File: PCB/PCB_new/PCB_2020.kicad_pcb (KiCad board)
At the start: 2 copper layers, 102.2 x 94.5 mm, 26 parts, among them IC1 LM358N, Q1 220mA/50V/3.5Ω, Q2 100V/17A, Q3 100V/17A, Q4 100V/17A, Q5 100V/17A, Q6 100V/17A, U1 TI_CONN

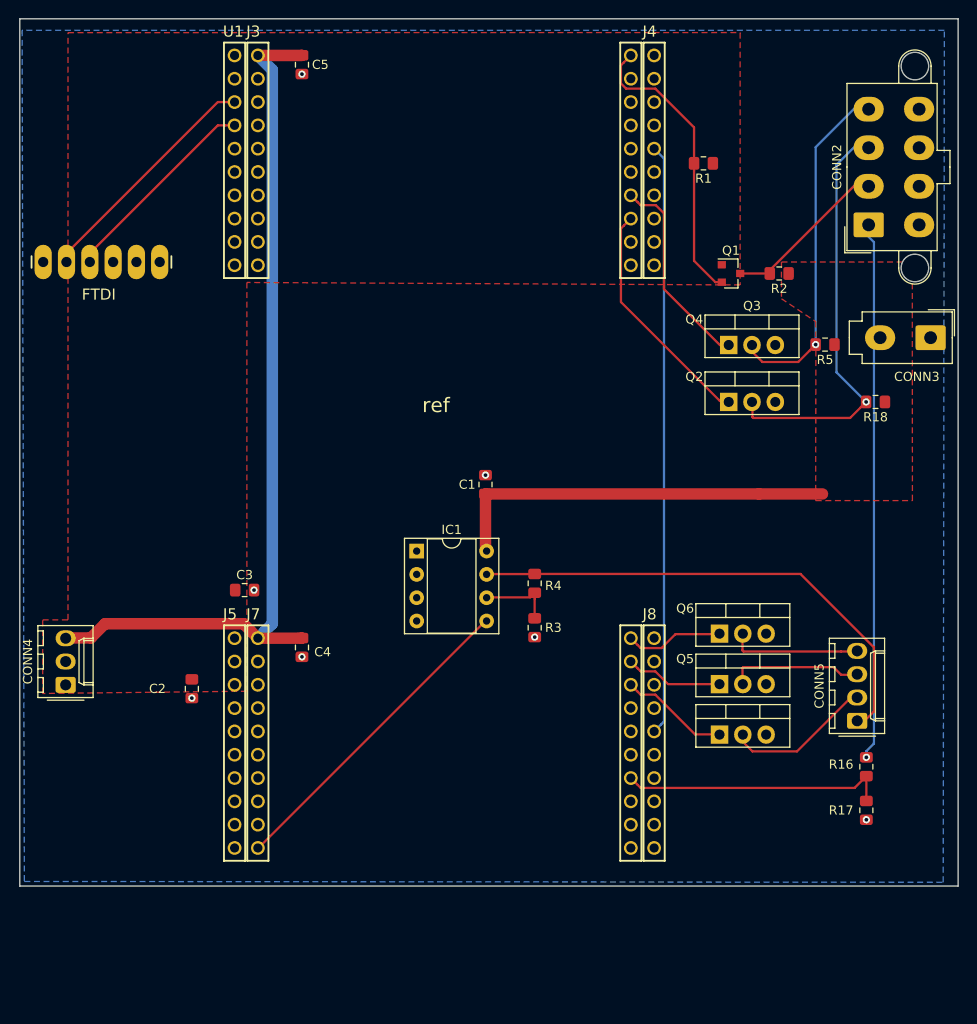
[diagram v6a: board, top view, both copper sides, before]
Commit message: moved components to keep proper space for ti
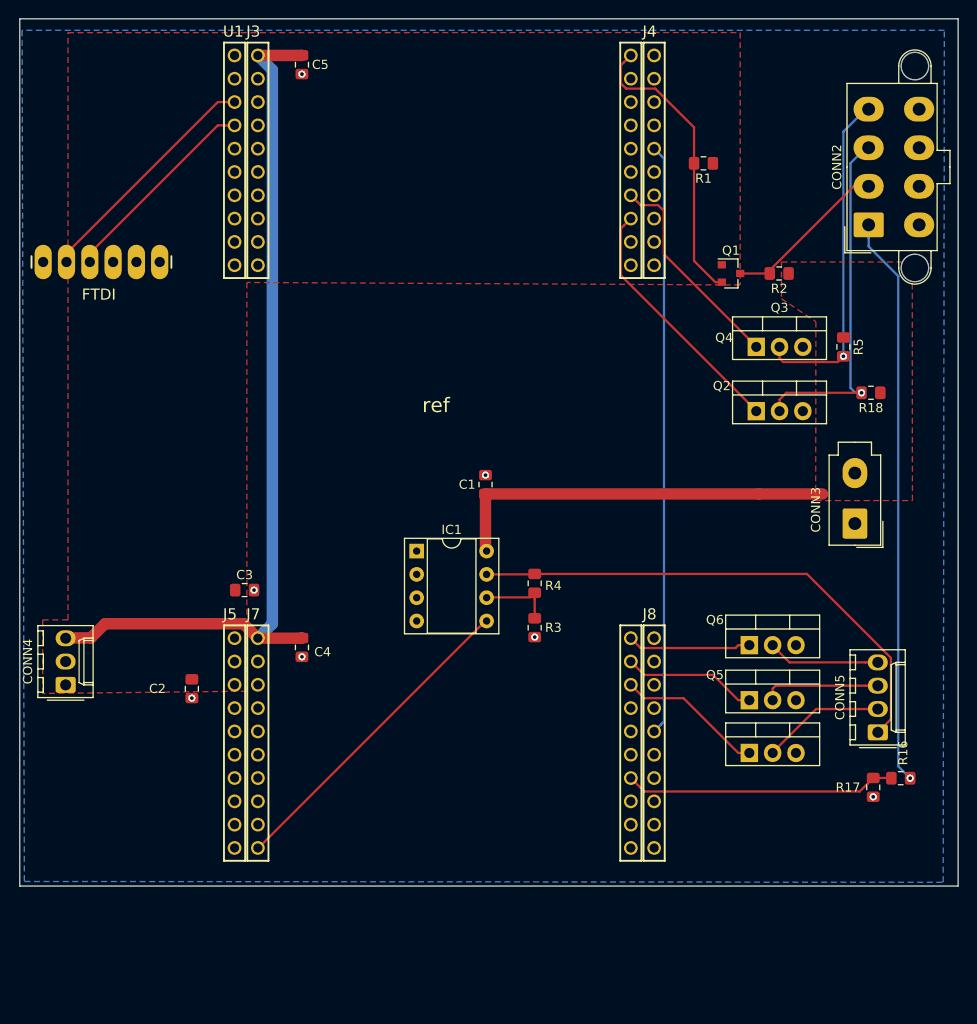
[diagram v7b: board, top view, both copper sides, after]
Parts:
- moved CONN3 21.9 mm to (186.8, 101.8), turned to 180 degrees
- moved R16 3.95 mm to (191.8, 129.5), turned to 180 degrees
- moved Q4 3.82 mm to (175.2, 126.8)
- moved Q5 3.69 mm to (175.2, 121.0)
- moved Q6 3.48 mm to (175.2, 115.0)
- moved Q2 3.16 mm to (176.0, 89.5)
- moved Q3 3.01 mm to (176.0, 82.5)
- moved R17 2.61 mm to (188.8, 130.5)
- moved CONN5 2.57 mm to (189.2, 124.5)
- moved R5 2.02 mm to (185.5, 82.5), turned to 270 degrees
- moved R18 1.12 mm to (188.5, 87.5)
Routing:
- net /LAUNCHXL-F28379D Breakout/INPUT_A+: track 46.2 -> 38.4 mm
- net REV_CTL: track 11.9 -> 16.0 mm
- net FWD_CTL: track 10.6 -> 14.7 mm
- net /LAUNCHXL-F28379D Breakout/HLFB+: track 58.8 -> 62.2 mm
- net FS1_CTL: track 10.7 -> 13.5 mm
- net /LAUNCHXL-F28379D Breakout/REV_MC: track 16.1 -> 13.5 mm
- net /LAUNCHXL-F28379D Breakout/FS1_MC: track 14.3 -> 12.3 mm
- net /LAUNCHXL-F28379D Breakout/FWD_MC: track 14.6 -> 12.8 mm
- net INPUT_A+_CTL: track 25.8 -> 27.5 mm
- net /LAUNCHXL-F28379D Breakout/THROTTLE_MC: track 54.9 -> 56.6 mm
- net EN+_CTL: track 22.3 -> 23.3 mm
- net /LAUNCHXL-F28379D Breakout/EN+: track 37.8 -> 36.9 mm
